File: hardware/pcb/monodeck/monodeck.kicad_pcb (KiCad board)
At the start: 2 copper layers, 71 x 53.8 mm, 13 parts

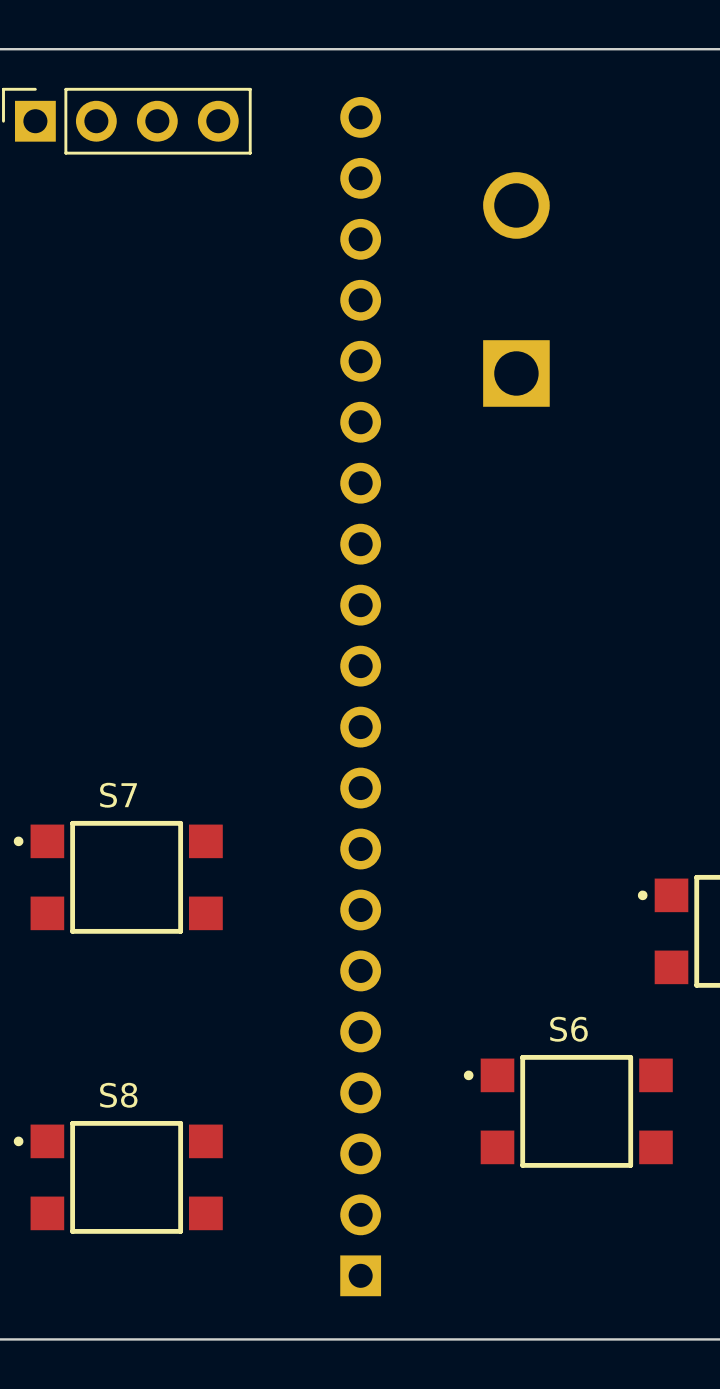
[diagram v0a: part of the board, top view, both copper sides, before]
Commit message: updated schematic and pcb, replaced pico smd with pin sockets
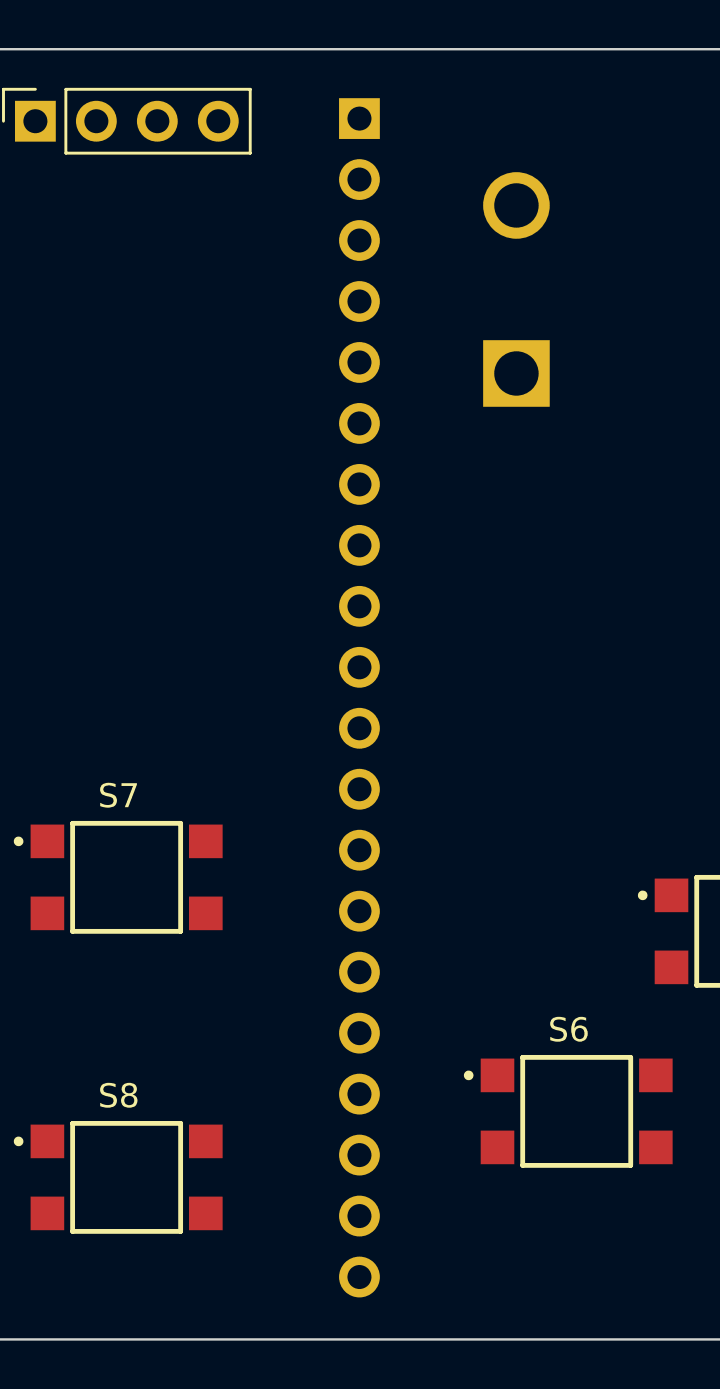
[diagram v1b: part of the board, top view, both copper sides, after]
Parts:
- removed REF** (x2): PinSocket_1x20_P2.54mm_Vertical, Connector_PinSocket_2.54mm:PinSocket_1x20_P2.54mm_Vertical
- added J1: Conn_01x20_Socket, Connector_PinSocket_2.54mm:PinSocket_1x20_P2.54mm_Vertical, B.Cu at (157.5, 103.1)
- added J2: Conn_01x20_Socket, Connector_PinSocket_2.54mm:PinSocket_1x20_P2.54mm_Vertical, B.Cu at (176.9, 54.9)
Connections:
- OLED1 pad 3: /SCL -> /GPIO9
- OLED1 pad 4: /SDA -> /GPIO8

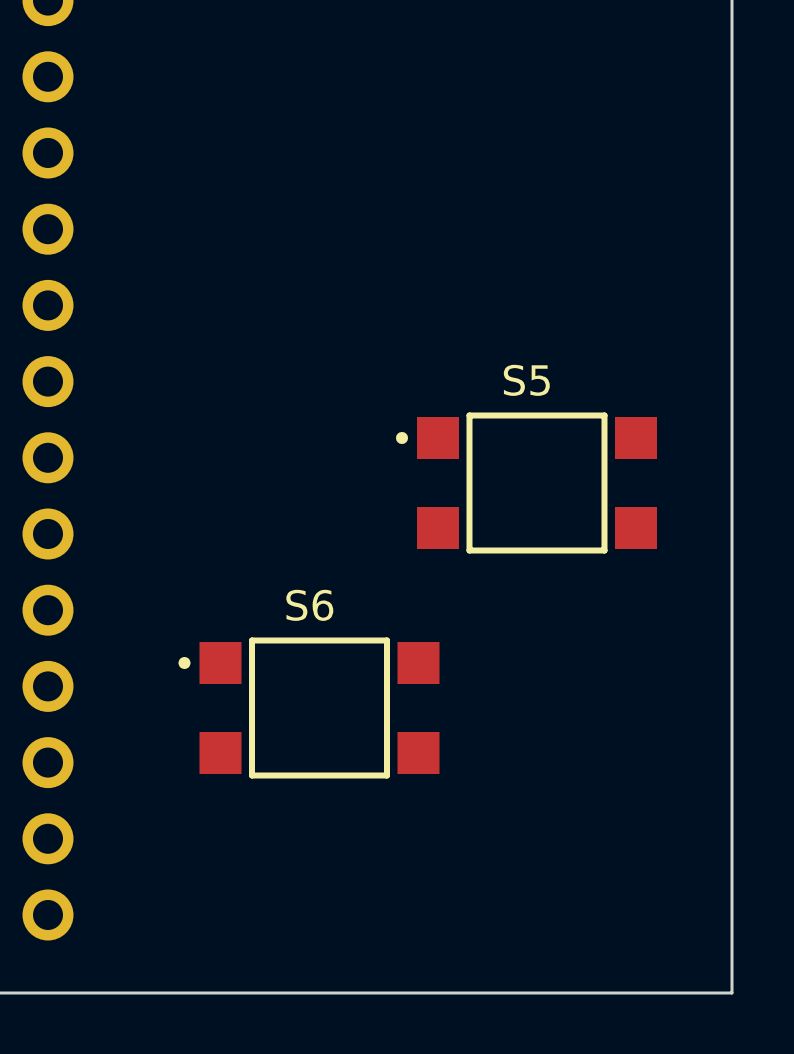
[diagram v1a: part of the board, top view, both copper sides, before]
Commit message: added tp4056 module to the circuit
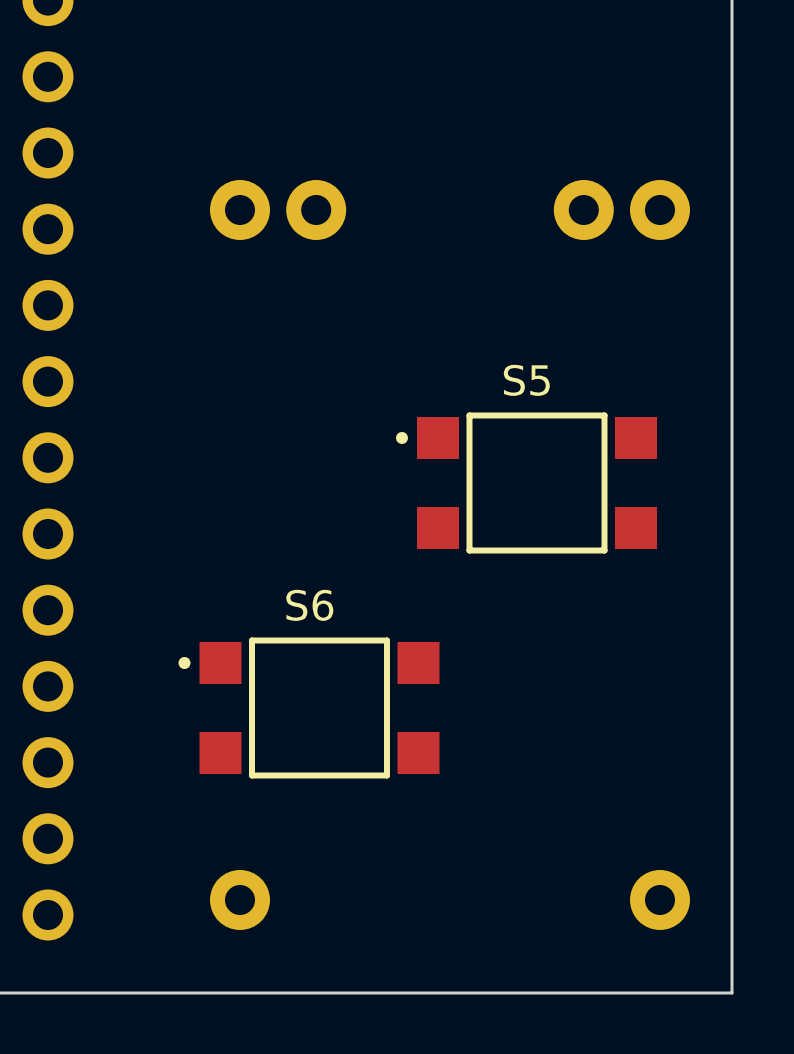
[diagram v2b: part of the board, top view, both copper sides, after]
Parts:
- added U1: TP4056, TP4056-Module:TP4056-Module, B.Cu at (181.8, 105.2)
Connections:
- BAT1 pad 1: /V+ -> Net-(BAT1-Pin_1)
- J2 pad 20: Net-(J2-VBUS) -> /V+
- PWR1 pad 1: Net-(J2-VBUS) -> Net-(U1-Vout+)
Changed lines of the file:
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@@
 	(net 36 "unconnected-(J1-GP3-Pad5)")
 	(net 37 "unconnected-(J1-GP5-Pad7)")
-	(net 38 "Net-(J2-VBUS)")
+	(net 38 "Net-(BAT1-Pin_1)")
 	(net 39 "unconnected-(J2-ADC_VREF-Pad15)")
 	(net 40 "unconnected-(J2-GP22-Pad9)")
@@
 	(net 49 "unconnected-(J2-GP28-Pad14)")
 	(net 50 "unconnected-(J2-VSYS-Pad19)")
+	(net 51 "Net-(U1-Vout+)")
+	(net 52 "unconnected-(U1-Vin+-Pad1)")
+	(net 53 "unconnected-(U1-Vin--Pad2)")
 	(footprint "SWT0211-050010GSA_REVA:SW_SWT0211-050010GSA_REVA"
 		(layer "F.Cu")
@@
 		(embedded_fonts no)
 	)
+	(footprint "TP4056-Module:TP4056-Module"
+		(layer "B.Cu")
+		(at 181.75 105.15 90)
+		(property "Reference" "U1"
+			(at 13.97 10.644 270)
+			(unlocked yes)
+			(layer "B.SilkS")
+			(effects
+				(font
+					(size 1 1)
+					(thickness 0.1)
+				)
+				(justify mirror)
+			)
+		)
+		(property "Value" "TP4056"
+			(at 13.97 9.144 270)
+			(unlocked yes)
+			(layer "B.Fab")
+			(effects
+				(font
+					(size 1 1)
+					(thickness 0.15)
+				)
+				(justify mirror)
+			)
+		)
+		(property "Datasheet" ""
+			(at 0 0 270)
+			(unlocked yes)
+			(layer "B.Fab")
+			(hide yes)
+			(effects
+				(font
+					(size 1 1)
+					(thickness 0.15)
+				)
+				(justify mirror)
+			)
+		)
+		(property "Description" ""
+			(at 0 0 270)
+			(unlocked yes)
+			(layer "B.Fab")
+			(hide yes)
+			(effects
+				(font
+					(size 1 1)
+					(thickness 0.15)
+				)
+				(justify mirror)
+			)
+		)
+		(sheetname "/")
+		(sheetfile "monodeck.kicad_sch")
+		(attr smd)
+		(fp_line
+			(start 0 0)
+			(end 28 0)
+			(stroke
+				(width 0.1)
+				(type solid)
+			)
+			(layer "B.SilkS")
+		)
+		(fp_line
+			(start 28 17.2)
+			(end 28 0)
+			(stroke
+				(width 0.1)
+				(type default)
+			)
+			(layer "B.SilkS")
+		)
+		(fp_line
+			(start 0 17.2)
+			(end 0 0)
+			(stroke
+				(width 0.1)
+				(type default)
+			)
+			(layer "B.SilkS")
+		)
+		(fp_line
+			(start 0 17.2)
+			(end 28 17.2)
+			(stroke
+				(width 0.1)
+				(type solid)
+			)
+			(layer "B.SilkS")
+		)
+		(fp_text user "${REFERENCE}"
+			(at 13.97 7.644 270)
+			(unlocked yes)
+			(layer "B.Fab")
+			(effects
+				(font
+					(size 1 1)
+					(thickness 0.15)
+				)
+				(justify mirror)
+			)
+		)
+		(pad "1" thru_hole circle
+			(at 2.5 15.6 90)
+			(size 2 2)
+			(drill 1)
+			(layers "*.Cu" "*.Mask")
+			(remove_unused_layers no)
+			(net 52 "unconnected-(U1-Vin+-Pad1)")
+			(pinfunction "Vin+")
+			(pintype "power_in+no_connect")
+		)
+		(pad "2" thru_hole circle
+			(at 2.5 1.6 90)
+			(size 2 2)
+			(drill 1)
+			(layers "*.Cu" "*.Mask")
+			(remove_unused_layers no)
+			(net 53 "unconnected-(U1-Vin--Pad2)")
+			(pinfunction "Vin-")
+			(pintype "power_in+no_connect")
+		)
+		(pad "3" thru_hole circle
+			(at 25.5 15.6 90)
+			(size 2 2)
+			(drill 1)
+			(layers "*.Cu" "*.Mask")
+			(remove_unused_layers no)
+			(net 51 "Net-(U1-Vout+)")
+			(pinfunction "Vout+")
+			(pintype "power_out")
+		)
+		(pad "4" thru_hole circle
+			(at 25.5 1.6 90)
+			(size 2 2)
+			(drill 1)
+			(layers "*.Cu" "*.Mask")
+			(remove_unused_layers no)
+			(net 1 "GND")
+			(pinfunction "Vout-")
+			(pintype "power_out")
+		)
+		(pad "5" thru_hole circle
+			(at 25.5 13.06 90)
+			(size 2 2)
+			(drill 1)
+			(layers "*.Cu" "*.Mask")
+			(remove_unused_layers no)
+			(net 38 "Net-(BAT1-Pin_1)")
+			(pinfunction "B+")
+			(pintype "power_in")
+		)
+		(pad "6" thru_hole circle
+			(at 25.5 4.14 90)
+			(size 2 2)
+			(drill 1)
+			(layers "*.Cu" "*.Mask")
+			(remove_unused_layers no)
+			(net 1 "GND")
+			(pinfunction "B-")
+			(pintype "power_in")
+		)
+		(embedded_fonts no)
+	)
 	(footprint "R1966ABLKBLKGR:SW_R1966ABLKBLKGR"
 		(layer "B.Cu")
@@
 			(layers "*.Cu" "*.Mask")
 			(remove_unused_layers no)
-			(net 38 "Net-(J2-VBUS)")
+			(net 51 "Net-(U1-Vout+)")
 			(pintype "passive")
 			(solder_mask_margin 0.102)
@@
 			(remove_unused_layers no)
 			(roundrect_rratio 0.208333)
-			(net 14 "/V+")
+			(net 38 "Net-(BAT1-Pin_1)")
 			(pinfunction "Pin_1")
 			(pintype "passive")
@@
 			(layers "*.Cu" "*.Mask")
 			(remove_unused_layers no)
-			(net 38 "Net-(J2-VBUS)")
+			(net 14 "/V+")
 			(pinfunction "VBUS")
 			(pintype "passive")

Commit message: finished first iteration of pcb
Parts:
- moved PWR1 1.00 mm to (184.5, 65.5)
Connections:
- J1 pad 13: GND -> unconnected-(J1-GND-Pad13)
- J1 pad 3: GND -> GND1
- J1 pad 4: unconnected-(J1-GP2-Pad4) -> /GPIO2
- J1 pad 5: unconnected-(J1-GP3-Pad5) -> /GPIO3
- J1 pad 8: GND -> unconnected-(J1-GND-Pad8)
- J2 pad 13: GND -> unconnected-(J2-GND-Pad13)
- J2 pad 18: GND -> GND2
- S1 pad 1: unconnected-(S1-Pad1) -> GND1
- S1 pad 2: GND -> unconnected-(S1-Pad2)
- S2 pad 1: unconnected-(S2-Pad1) -> GND1
- S2 pad 2: GND -> GND1
- S2 pad 3: unconnected-(S2-Pad3) -> /GPIO11
- S2 pad 4: /GPIO11 -> unconnected-(S2-Pad4)
- S3 pad 1: unconnected-(S3-Pad1) -> GND1
- S3 pad 2: GND -> unconnected-(S3-Pad2)
- S4 pad 2: GND -> GND1
- S4 pad 3: unconnected-(S4-Pad3) -> /GPIO13
- S4 pad 4: /GPIO13 -> unconnected-(S4-Pad4)
- S5 pad 1: unconnected-(S5-Pad1) -> /GPIO20
- S5 pad 2: /GPIO14 -> unconnected-(S5-Pad2)
- S5 pad 4: GND -> GND2
- S6 pad 1: unconnected-(S6-Pad1) -> /GPIO21
- S6 pad 2: /GPIO15 -> unconnected-(S6-Pad2)
- S6 pad 4: GND -> GND2
- S7 pad 2: GND -> GND2
- S7 pad 3: unconnected-(S7-Pad3) -> /GPIO3
- S7 pad 4: /GPIO20 -> unconnected-(S7-Pad4)
- S8 pad 2: GND -> GND2
- S8 pad 3: unconnected-(S8-Pad3) -> /GPIO2
- S8 pad 4: /GPIO21 -> unconnected-(S8-Pad4)
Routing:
- net Net-(BAT1-Pin_1): track 0.00 -> 76.9 mm
- net GND: track 0.00 -> 70.7 mm
- net /V+: track 0.00 -> 70.5 mm
- net GND2: track 0.00 -> 59.6 mm
- net /GPIO13: track 0.00 -> 55.0 mm
- net /GPIO11: track 0.00 -> 49.1 mm
- net /VCC: track 0.00 -> 44.1 mm
- net GND1: track 0.00 -> 43.8 mm
- net /GPIO12: track 0.00 -> 38.1 mm
- net /GPIO8: track 0.00 -> 29.1 mm
- net /GPIO21: track 0.00 -> 27.0 mm
- net /GPIO20: track 0.00 -> 26.3 mm
- net /GPIO9: track 0.00 -> 26.1 mm
- net /GPIO10: track 0.00 -> 24.2 mm
- net Net-(U1-Vout+): track 0.00 -> 19.5 mm
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- added copper zone on B.Cu, net GND
- added copper zone on F.Cu, net GND
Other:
- board size 71 x 53.8 mm -> 72 x 54.8 mm
